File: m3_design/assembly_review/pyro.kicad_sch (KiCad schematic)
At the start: 22 parts, among them J121 IGNITER 1: E1- / E1+, J124 ARM CH1: BUS1 / RAW, Q124 AON7524

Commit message: R10: m3_design/r10_build.sh and per-family stage gate; m3_design/assembly_review rebuilt as M3-ASSY-R10 (board 883d2db5..., 46 x 90 mm); tools/check.sh passes at zero; binding note bound to the board
Co-Authored-By: Claude Opus 5.5 <noreply@anthropic.com>
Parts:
- J121: value IGNITER 1: E1- / E1+ -> DB125-3.5-2P-BK-S; footprint rocket:M3_DB128L_2P_BK_SW -> rocket:M3_DB125_2P_BK; LCSC C430601 -> C52993880; LCSC Part C430601 -> (none); Manufacturer Part DB128L-5.08-2P-BK-S -> DB125-3.5-2P-BK-S
- J124: value ARM CH1: BUS1 / RAW -> DB125-3.5-2P-BK-S; footprint rocket:M3_DB128L_2P_BK_SW -> rocket:M3_DB125_2P_BK; LCSC C430601 -> C52993880; LCSC Part C430601 -> (none); Manufacturer Part DB128L-5.08-2P-BK-S -> DB125-3.5-2P-BK-S
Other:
- note added: "ARM plug is the complete electrical break: fit last, remove first. Black3.5mm terminals enter from -x; direct J124 pad/copper gap >=1.5mm."
- note added: "Ground ARM/continuity checks refuse firing; in flight readings only log/annunciate and never veto a fire. Firmware fire timeout <=20ms."
- note added: "R10 uses default board clearance; accepted loss of R9 single-defect spacing margins does not waive functional reset, gate or divider safety."
- note added: "R10: one recovery channel, unchanged functional fire/gate/sense network. J124.2 RAW_ACT, J124.1 BUS; J121.2 IGN, J121.1 OUT."
- note removed: "12 | Single pyro CH1, arming and continuity"
- note removed: "CONT: R173 + R129 over R130 || R178 from drain. ARM: R132 + R175 over R133 || R180 from fused bus."
- note removed: "D120 cathode 1 + R131 10k: cold pull-up for plug-out FET-short detection. Cathode 2 NC. In flight: log only, never veto."
- note removed: "Gate: MCU -> 220R -> gate; 1k pull-down on MCU side; 10k + 220nF gate-source (P0-1/P0-2). Off in reset/unpowered."
- note removed: "Igniter across J121.1 OUT and J121.2 IGN. J124 and J121 pin numbering (the net on each pin) is retained from the reviewed CH1. R9: both on M3_DB128L_2P_BK_SW (the DB128L with pads 1 and 2 swapped: same part C430601, same land), turned so both wires enter from -x (pyro leads west) with pin 2 (RAW / IGN) forward and pin 1 (BUS / OUT) aft."
- note removed: "One pyro channel. J124.2 RAW -> external F1 5A FAST -> J124.1 BUS1. Black J124 ARM / J121 IGN; identify by silk and pin legends."
- note removed: "PE3 (pin 2) and PE6 (pin 5) are sentinels with no net: firmware drives them low. Never enable TRACE on PE2-PE6."
- note removed: "R134: 2 ohm 2 W pulse-rated Bourns CRM2512; shorted-igniter current about 4 A. Firmware fire pulse <= 20 ms."
- note removed: "Split divider tops: R173 + R129 and R132 + R175 (2 x 5.1k). Bottoms: R130 || R178 and R133 || R180 (2 x 2k). Ratio 1/11.2. R168/R170 4.7k at MCU. CH1 coating and safety rules A-H/A2 remain mandatory."
- note removed: "With the ARM plug out NOTHING connects RAW_ACT to PYRO1_BUS. No test point on BUS, IGN or OUT."

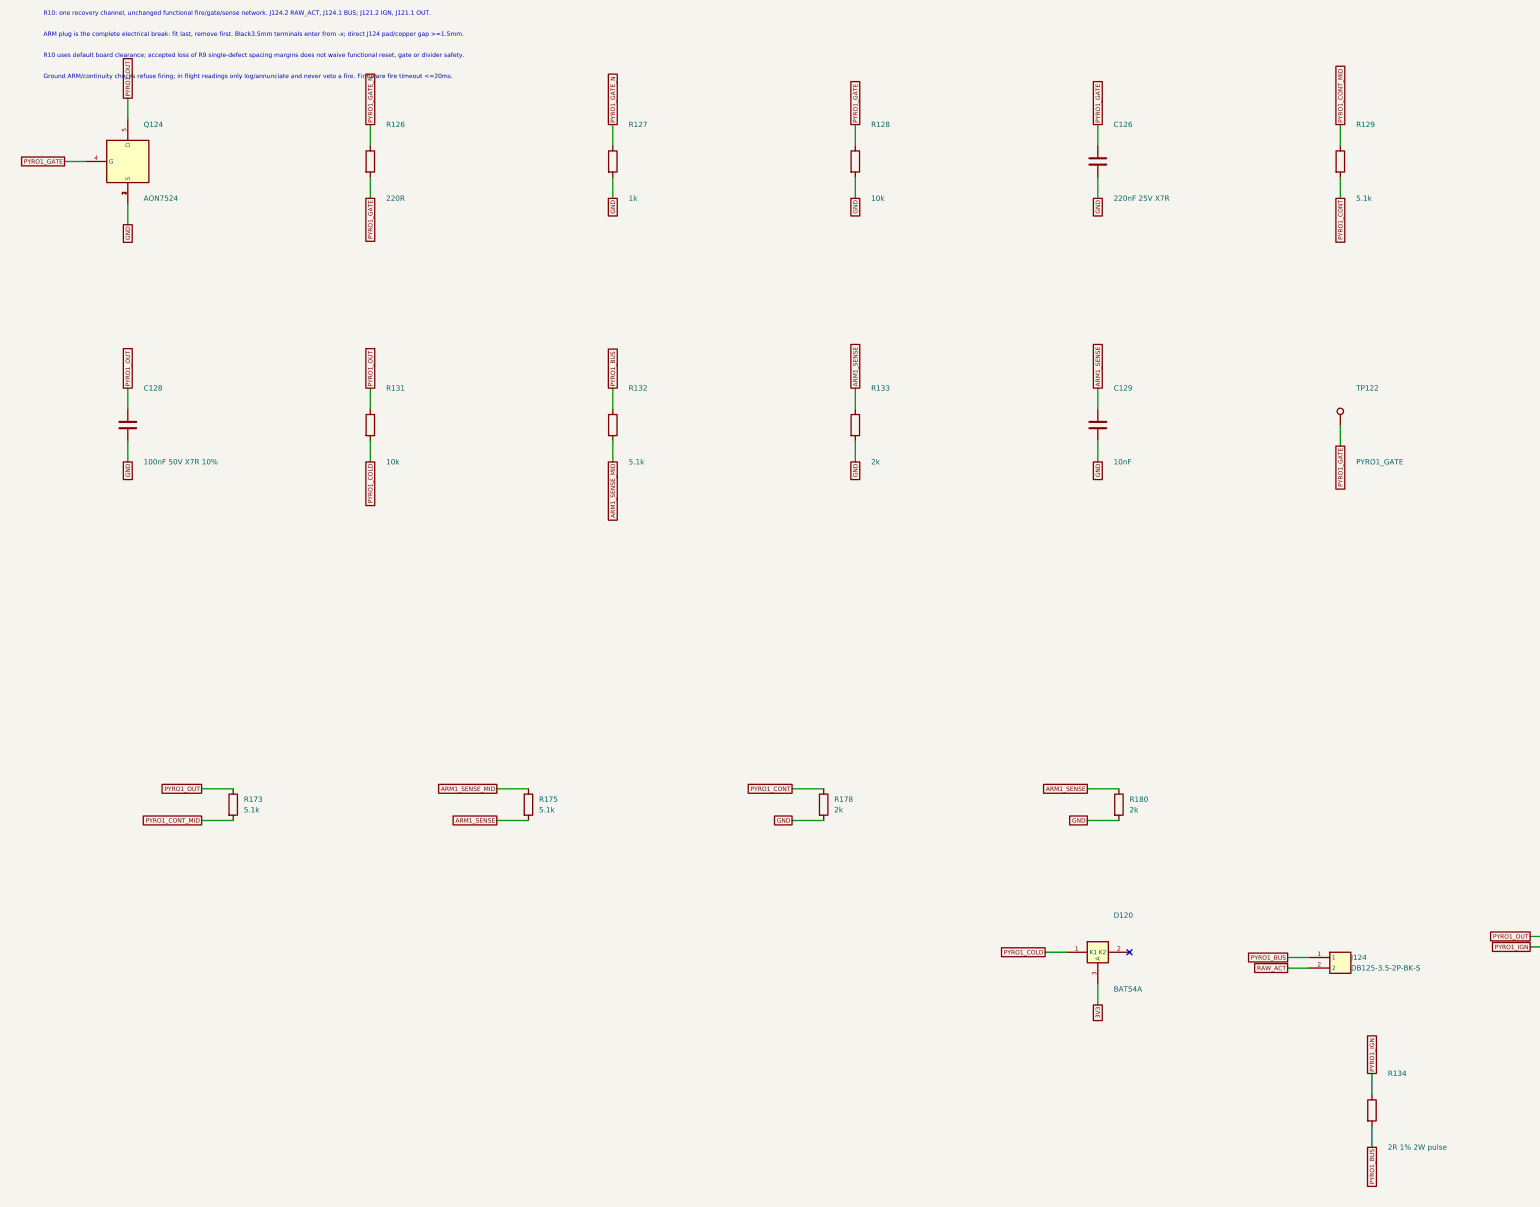
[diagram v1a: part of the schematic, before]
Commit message: R10 single screw-switch arming pass before review round 9
Preparatory single-switch pass, not a full review round or clean-round credit.
Remove J124 and its fused ARM link, join the post-switch bus as RAW_ACT, and
implement the independent PC1 load-switch enable through R122/Q122 while PE4
controls the fire FET. Move R134 for direct bottom-side fire routing. Update
schematic/PCB generators, contracts, seeded tests, binding and operating records.
No interrupted changes were discarded. AUD/GAP cuts and fresh round 9 follow.

Board SHA-256: 60be35eaff86dd7a5fb8e065aa4204a51e7d786d7dfc8d2456cdd66c4b86f901
Board: 46 x 90 mm, 4 layers, 2521622 bytes. Two full builds are byte-identical.
Netlist SHA-256: 3e08722d7ac997131cb11d7c9cb2d25e1b3babcfb853b71230db01118bc70e69
Fab: 228 CPL rows, 83 BOM lines; orientation, paste and manifest checks pass.
Hot-plug: same input-feed signature; 2304 corners and local sensitivities pass
(simulation / Inference). Bench, firmware, RF immunity and physical fit unverified.

Final unskipped tools/check.sh: exit 0
DRC violations 0  unconnected 0  schematic parity 0  ERC 0
metadata / 3D model audit: OK
fit check: OK (CAD envelopes only)
R10 CAD contract (full): OK
routing hygiene: 0 failing, 0 allowlisted, 0 leftovers recorded
actuator safety contract: OK
Fab manifest: OK; 5 outputs match the current CAD and export inputs
Self-tests: shell 4, fit 23, paste 5, route 57; R10 122 (3 NumPy tests
skipped in KiCad Python then passed separately). Standalone plate 3 passed.
Added local absolute paths: 0. No direct Git index/commit mutation performed.

Co-Authored-By: Claude Opus 5.5 <noreply@anthropic.com>
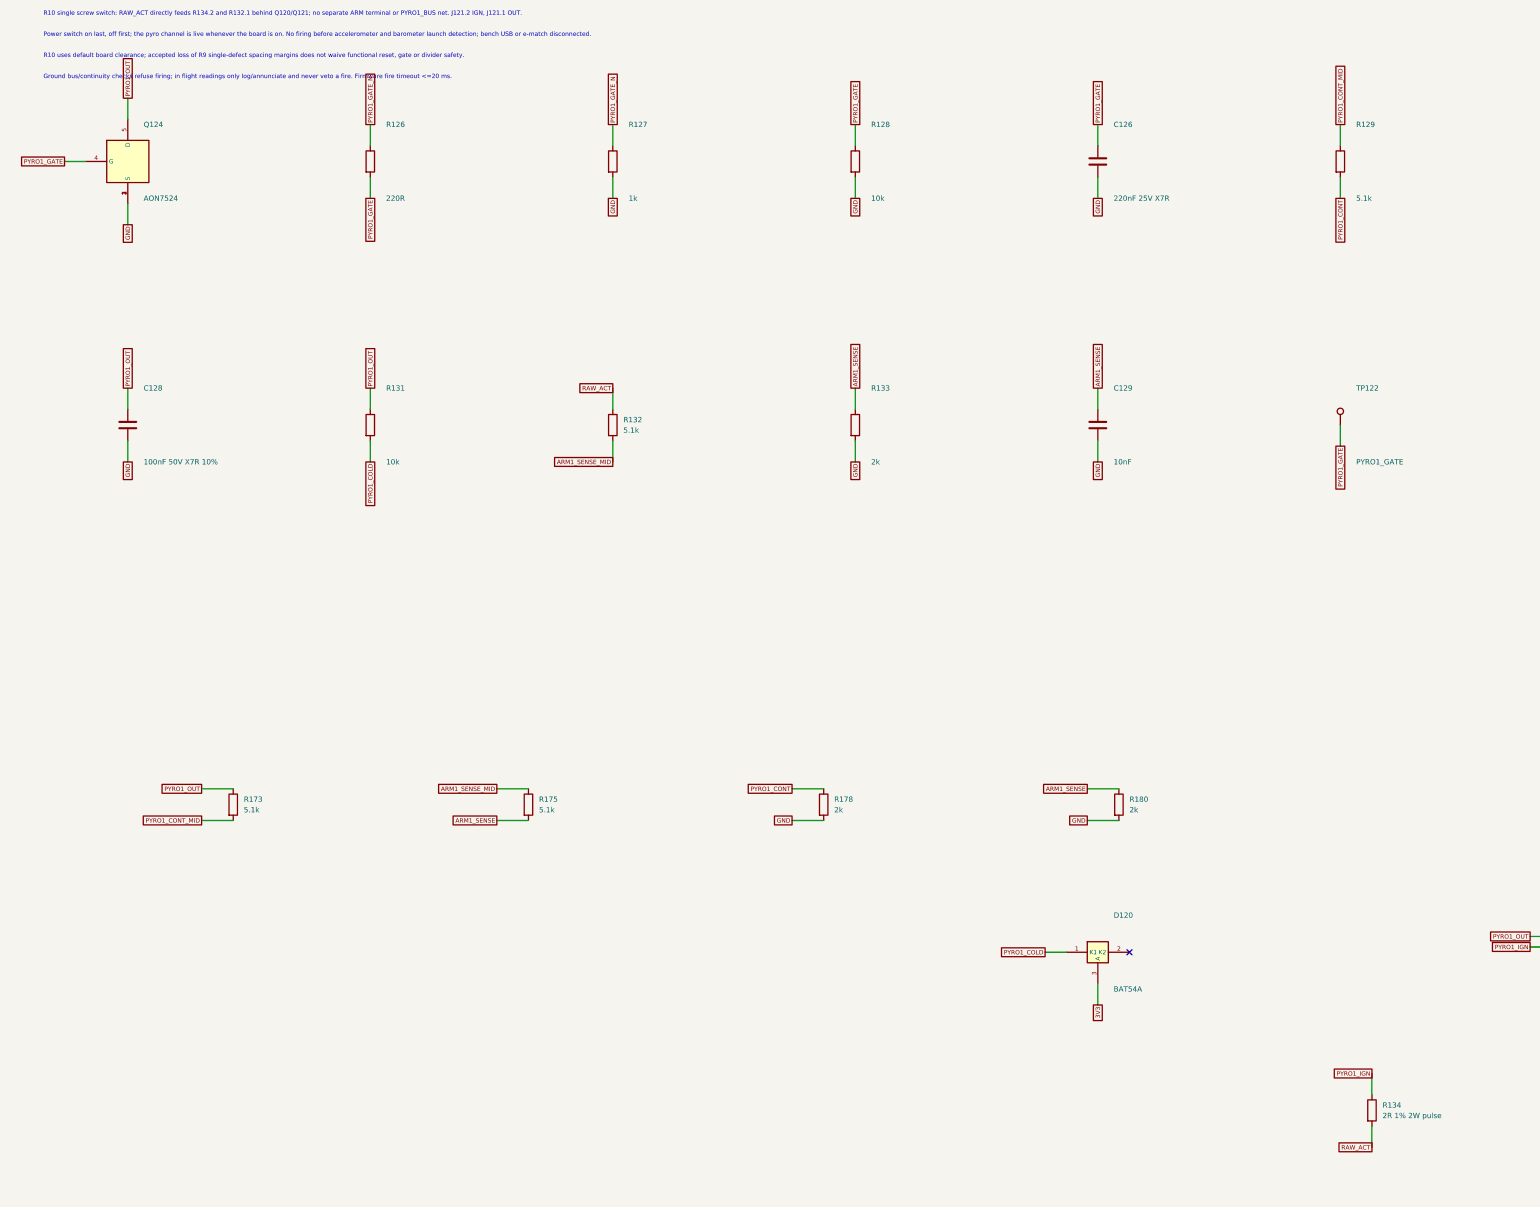
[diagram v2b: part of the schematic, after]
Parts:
- removed J124: DB125-3.5-2P-BK-S, rocket:M3_DB125_2P_BK, symbol M3:Conn_1x2
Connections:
- net PYRO1_BUS is gone; now on net RAW_ACT: R132.1, R134.2
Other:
- note added: "Ground bus/continuity checks refuse firing; in flight readings only log/annunciate and never veto a fire. Firmware fire timeout <=20 ms."
- note added: "Power switch on last, off first; the pyro channel is live whenever the board is on. No firing before accelerometer and barometer launch detection; bench USB or e-match disconnected."
- note added: "R10 single screw switch: RAW_ACT directly feeds R134.2 and R132.1 behind Q120/Q121; no separate ARM terminal or PYRO1_BUS net. J121.2 IGN, J121.1 OUT."
- note removed: "ARM plug is the complete electrical break: fit last, remove first. Black3.5mm terminals enter from -x; direct J124 pad/copper gap >=1.5mm."
- note removed: "Ground ARM/continuity checks refuse firing; in flight readings only log/annunciate and never veto a fire. Firmware fire timeout <=20ms."
- note removed: "R10: one recovery channel, unchanged functional fire/gate/sense network. J124.2 RAW_ACT, J124.1 BUS; J121.2 IGN, J121.1 OUT."

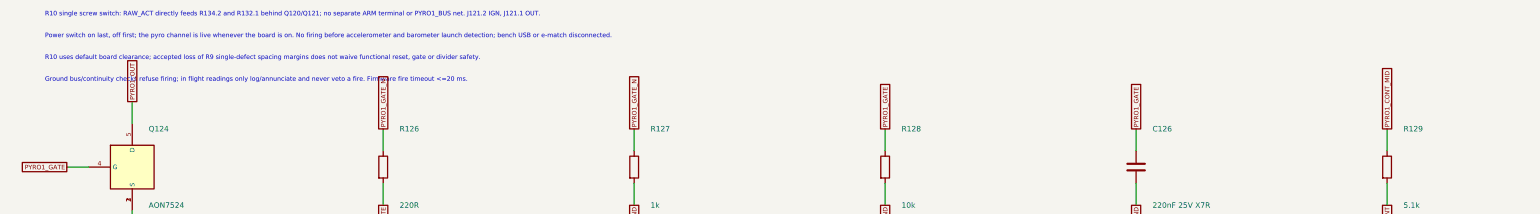
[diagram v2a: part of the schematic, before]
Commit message: R10 requirements-audit cuts and GAP fixes before review round 9
Implement adopted AUD-1 through AUD-10 and GAP-1 through GAP-5 after the single-switch pass.
Remove the advisory pull-pin, redundant probes and GPS/radio IO LDO cells; qualify the smaller
AONR21357 pair, correct C120 voltage rating, standardize shared-code capacitor lands, simplify
slow returns and fire-only copper, localize U9 output protection and add exactly two U401 VIPPO vias.
Record physical-current timing, coupled fire/source budget, C84 manual fitting and narrowed gate scopes.

Board SHA-256: 877d01996a59e9dd5c6dbc367274bb9a323a13982d67960fe46df9b0ee53205d
Board: 46 x 90 mm, 4 layers, 2365477 bytes; 225 footprints, 883 straight tracks, 323 vias.
Netlist SHA-256: 0843da709e2d7a757e9b35cdff48158a54012c5353619cbf409ab961efd2c3ca
Two fresh complete passing builds are byte-identical. Schematic: 700 pins; 22 seeded faults detected.

Final unskipped tools/check.sh: exit 0
DRC violations 0  unconnected 0  schematic parity 0  ERC 0
metadata / 3D model audit: OK
silkscreen outside the board outline: 0 stroke points
fit check: OK (CAD envelopes only)
R10 CAD contract (full): OK
routing hygiene: 0 failing, 0 allowlisted, 0 leftovers recorded
actuator safety contract: OK
Fab manifest: OK; 5 outputs match current CAD and export inputs
Self-tests: shell 4, fit 24, paste 5, routing 59, R10 131; three NumPy cases rerun and passed.

Fab: 215 CPL rows, 82 BOM codes; orientation / paste / manifest pass. Hot-plug: 2304 required
cases plus convergence and controls pass (simulation / Inference). Plate f1 280.9 Hz (Inference).
Live JLC: $84.43 vs $84.41 target, 46 Extended codes; R430 / U4 short. Procurement exit 1 is a
disclosed OQ-3 / ordering deviation, not a CAD gate pass. No quote accepted or order placed.
Firmware, bench, thermal/transient correlation, process acceptance, installed RF immunity and physical fit unverified.

This preparatory pass earns no clean-review credit. Start fresh full ten-lens round 9 on th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
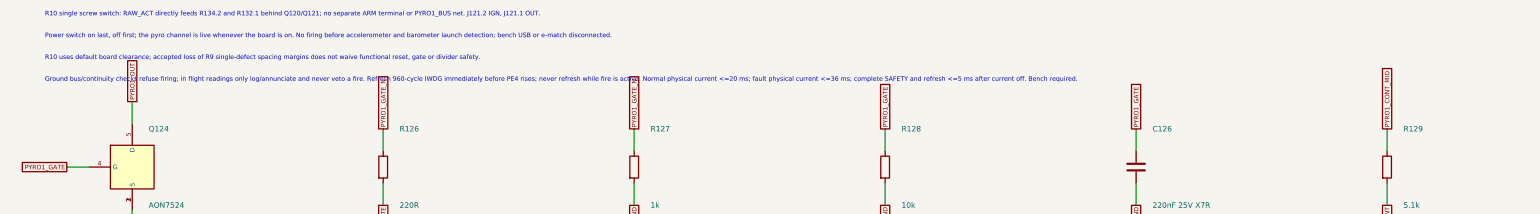
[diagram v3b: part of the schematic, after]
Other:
- note added: "Ground bus/continuity checks refuse firing; in flight readings only log/annunciate and never veto a fire. Refresh 960-cycle IWDG immediately before PE4 rises; never refresh while fire is active. Normal physical current <=20 ms; fault physical current <=36 ms; complete SAFETY and refresh <=5 ms after current off. Bench required."
- note removed: "Ground bus/continuity checks refuse firing; in flight readings only log/annunciate and never veto a fire. Firmware fire timeout <=20 ms."
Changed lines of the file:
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@@
 			(justify left))
 )
-	(text "Ground bus/continuity checks refuse firing; in flight readings only log/annunciate and never veto a fire. Firmware fire timeout <=20 ms."
+	(text "Ground bus/continuity checks refuse firing; in flight readings only log/annunciate and never veto a fire. Refresh 960-cycle IWDG immediately before PE4 rises; never refresh while fire is active. Normal physical current <=20 ms; fault physical current <=36 ms; complete SAFETY and refresh <=5 ms after current off. Bench required."
 		(at 20.32 30.48 0)
 		(effects
